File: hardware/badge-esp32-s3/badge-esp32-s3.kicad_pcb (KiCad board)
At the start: 2 copper layers, 131.5 x 83.5 mm, 121 parts, among them CN1 B4B-PH-SM4-TB (LF)(SN), CN2 ZX-SH1.0-4PWT, J1 Connector, USB-TYPE-C-16P, J2 Connector, USB-TYPE-C-16P, P1 PH-2A_C2319, Q1 SS8050 200-350, Q2 SS8050 200-350, Q3 HL2301A, SW1 TS-1088-AR02016, SW2 TS-1088-AR02016, U1 ESP32-S3-MINI-1-N8, U10 FH2.54-09-02PZD, U11 FH2.54-09-04PZD, U12 FH2.54-09-03PZD, U13 FH2.54-09-02PZD, U14 FH2.54-09-04PZD, U15 FH2.54-09-04PZD, U16 FH2.54-09-04PZD, U17 FH2.54-09-02PZD, U18 MMA8452QR1_C11360, U19 FH2.54-09-02PZD, U2 NCP167BMX330TBG, U3 CP2102N-A02-GQFN28R, U4 TP4056, U5 FH2.54-09-02PZD, U7 FH2.54-09-02PZD, U8 FH2.54-09-03PZD, U9 FH2.54-09-03PZD

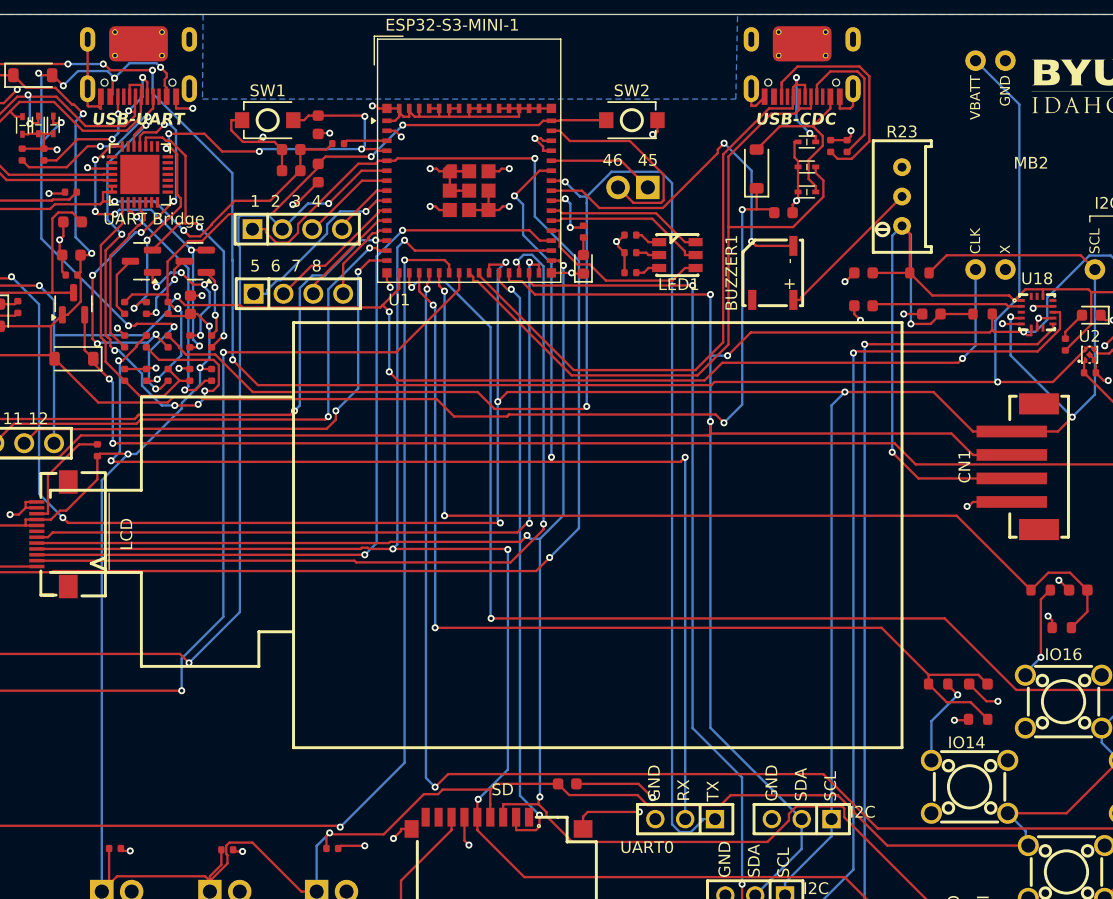
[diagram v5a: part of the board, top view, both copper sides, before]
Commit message: errors and warnings resolved
some warnings need to be addressed now and some errors are need to be rectified
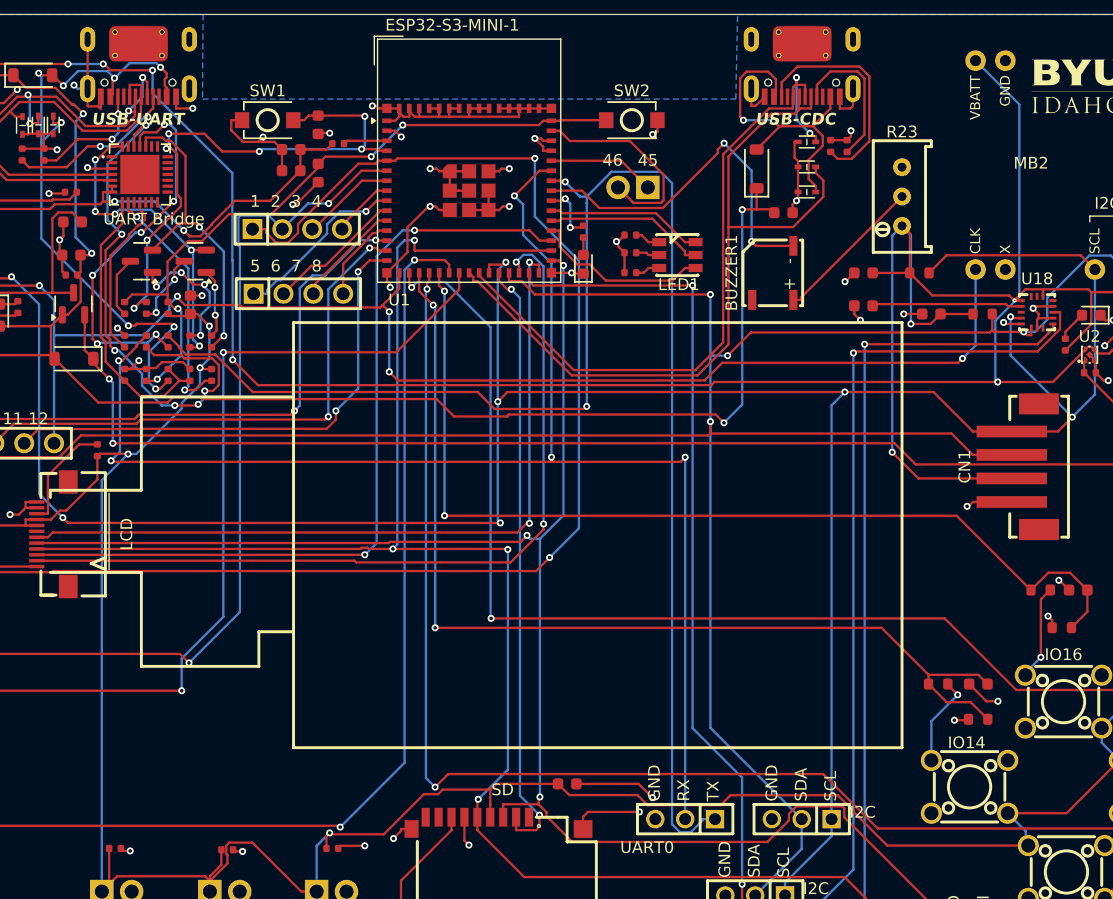
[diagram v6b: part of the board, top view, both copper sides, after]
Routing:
- net GND: track 216.8 -> 230.3 mm, vias 61 -> 60
- net /VBUSB: track 15.4 -> 27.5 mm, vias 0 -> 2

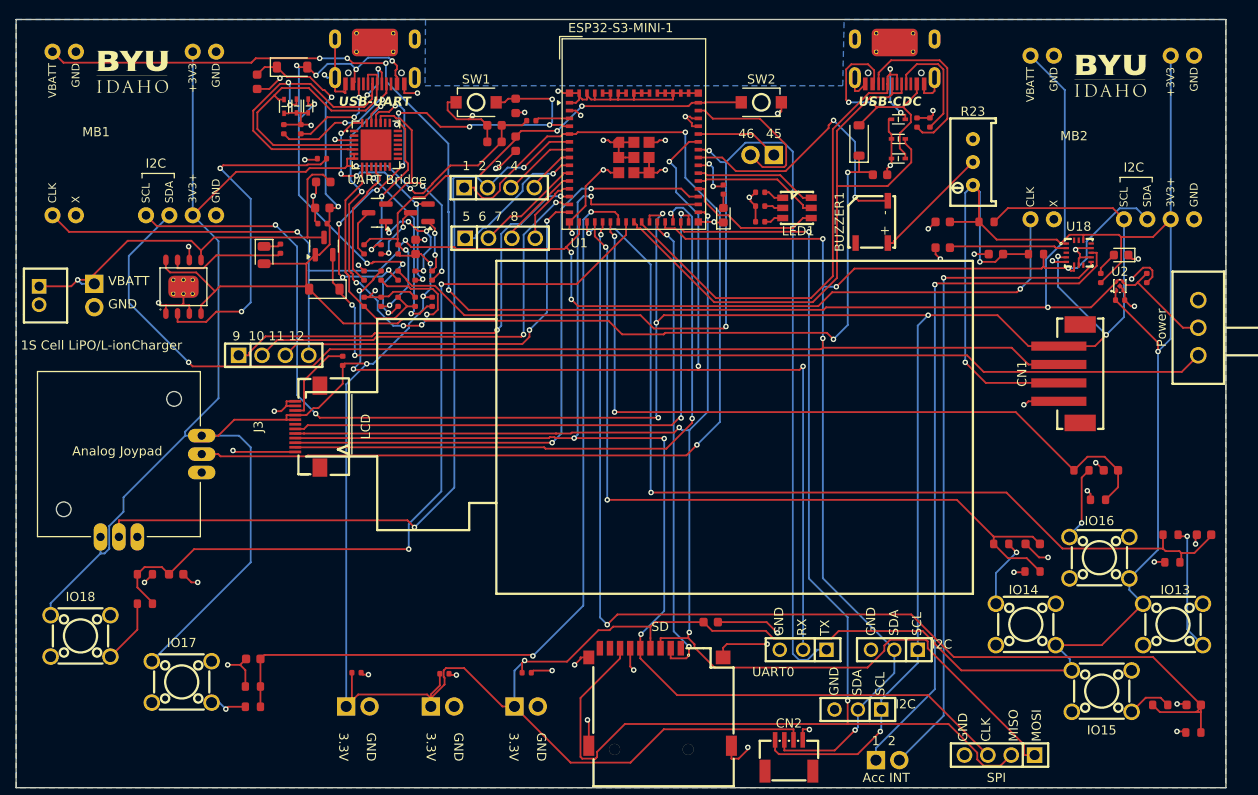
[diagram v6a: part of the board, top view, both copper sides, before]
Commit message: Fix additional DRC errors (5 left)
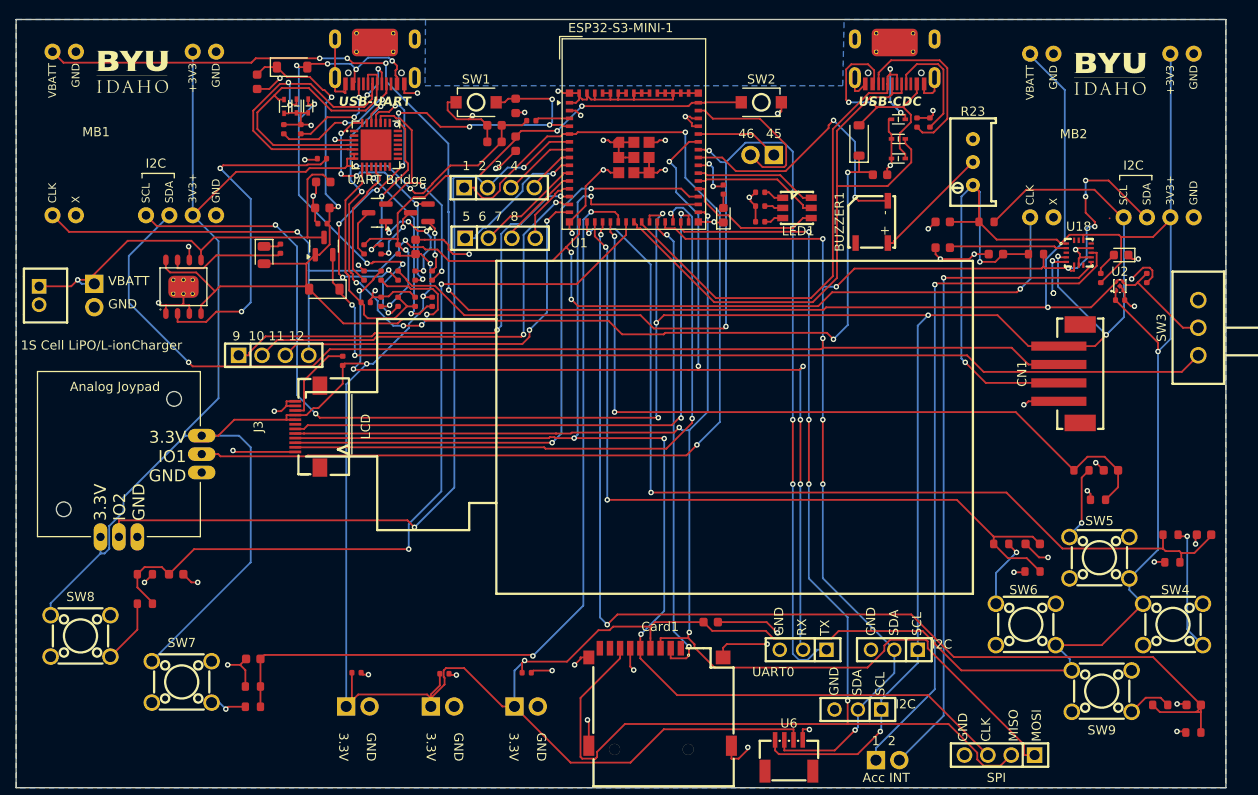
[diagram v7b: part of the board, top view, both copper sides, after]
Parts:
- moved MB2 0.22 mm to (192.4, 65.5)
- moved C8 0.19 mm to (121.5, 93.8), turned to 0 degrees
- renumbered SD to Card1, Power to SW3, IO13 to SW4, IO16 to SW5, IO14 to SW6, IO17 to SW7, IO18 to SW8, IO15 to SW9, CN2 to U6
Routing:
- net GND: track 230.3 -> 241.5 mm, vias 60 -> 61
- net /GPIO47: track 247.6 -> 255.2 mm, vias 6 -> 11
- net /GPIO21: track 251.7 -> 253.4 mm
- net /GPIO12: track 138.6 -> 139.7 mm
- net /VBUS: track 57.5 -> 56.8 mm
- net Net-(U3-VBUS): track 25.0 -> 25.5 mm
- net /U0RX: track 120.0 -> 120.3 mm, vias 5 -> 7
- net /U0TX: vias 2 -> 4
- net /GPIO34.: vias 2 -> 4
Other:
- board text added: "3.3V IO1 GND"
- board text added: "3.3V IO2 GND"

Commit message: First silkscreen version
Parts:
- added G***: LOGO, misc-lib:QRCodeFootPrint, B.Cu at (201.5, 78.5)
- moved R10 9.02 mm to (119.5, 82.0), turned to 180 degrees
- moved R11 5.78 mm to (120.0, 86.0), turned to -90 degrees
- renumbered CN1 to I2C, U6 to I2C, LED1 to RGB, SW1 to SWBOOT, SW2 to SWRESET
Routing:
- net Net-(U3-TXD): track 45.2 -> 21.0 mm, vias 6 -> 2
- net /GPIO34.: track 135.2 -> 155.2 mm, vias 4 -> 10
- net GND: track 241.5 -> 250.5 mm, vias 61 -> 59
- net Net-(U3-SUSPENDb): track 14.3 -> 5.38 mm
- net /U0RX: track 120.3 -> 125.6 mm, vias 7 -> 11
- net +3.3V: track 543.0 -> 537.9 mm, vias 9 -> 10
- net /VBUS: track 56.8 -> 61.6 mm, vias 8 -> 10
- net /GPIO1: track 120.0 -> 123.3 mm, vias 2 -> 6
- net Net-(U3-RXD): track 33.1 -> 36.3 mm, vias 6 -> 8
- net /U0TX: track 127.4 -> 130.2 mm, vias 4 -> 8
- net Net-(U3-VBUS): track 25.5 -> 28.2 mm
- net /GPIO12: track 139.7 -> 142.0 mm
- net /GPIO18: track 89.1 -> 91.2 mm, vias 2 -> 4
- net /GPIO47: track 255.2 -> 253.2 mm, vias 11 -> 13
- net /GPIO16: track 83.2 -> 81.3 mm
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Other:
- board text added: "Display Reset: 48 Data/Command: 37 (See SPI pins) Minibadge CLK: 12 (See I2C) Joystick (Optional) X axis: 1 Y axis: 2"
- board text added: "LED: 41 Buzzer: 42 RGB LED Red: 38 Green: 39 Blue: 40 Buttons Right: 13 Left: 14 Down: 15 Up: 16 B: 17 A: 18"
- board text added: "Peripherals"
- board text added: "Protocols"
- board text added: "UART TX: 43 RX: 44 SPI CLK: 32 MOSI: 31 MISO: 29 SD CS: 26 Display CS: 33 I2C SCL: 21 SDA: 47"
